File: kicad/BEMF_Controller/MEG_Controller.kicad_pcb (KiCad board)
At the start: 2 copper layers, 200 x 175 mm, 106 parts, among them J1 HEADER4VALULOK, J2 Recovery, J3 FUSE, J4 HEADER6, J5 Load, J7 Vin, Q1 C3M0280090D, Q2 C3M0280090D, Q3 C3M0280090D, Q4 C3M0280090D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

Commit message: Finished buck converter schematic
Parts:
- added C24: 100nF, Capacitor_SMD:C_0805_2012Metric, F.Cu at (381.6, 133.0)
- added C25: 6.8nF, Capacitor_SMD:C_0805_2012Metric, F.Cu at (381.6, 136.0)
- added L1: 33 uH, main:IND_BOURNS_SRN1060, F.Cu at (388.7, 113.2)
- added R1: 47k, Resistor_SMD:R_1206_3216Metric, F.Cu at (376.5, 133.1)
- added R10: 910, Resistor_SMD:R_1206_3216Metric, F.Cu at (376.5, 143.0)
- added R5: 10k, Resistor_SMD:R_1206_3216Metric, F.Cu at (376.5, 136.4)
- added R6: 20k, Resistor_SMD:R_1206_3216Metric, F.Cu at (376.5, 139.7)
- moved C69 14.1 mm to (113.8, 146.8), turned to 0 degrees
- moved C23 14.1 mm to (363.6, 90.2)
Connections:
- U1 pad 15: unconnected-(U1-PB7-Pad15) -> ConvEn
- U2 pad 3: unconnected-(U2-VC-Pad3) -> Net-(U2-VC)
- U2 pad 4: unconnected-(U2-FB-Pad4) -> /FB
- U2 pad 5: unconnected-(U2-RT-Pad5) -> Net-(U2-RT)
- U2 pad 6: unconnected-(U2-EN-Pad6) -> ConvEn
- U2 pad 7: unconnected-(U2-BST-Pad7) -> Net-(U2-BST)
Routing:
- net (no net): track 358.3 -> 22.9 mm, vias 12 -> 2
- net unconnected-(U8-OUTC-Pad13): track 191.5 -> 0.00 mm, vias 4 -> 0
- net unconnected-(U8-OUTB-Pad14): track 144.1 -> 0.40 mm, vias 4 -> 0
- net /Analog_IO/VSENSE_L_IN: track 199.7 -> 64.8 mm, vias 10 -> 6
- net /10V: track 143.4 -> 121.9 mm, vias 7 -> 5
- net GND: track 54.4 -> 44.3 mm, vias 226 -> 216
- net LOAD+: track 0.71 -> 0.00 mm

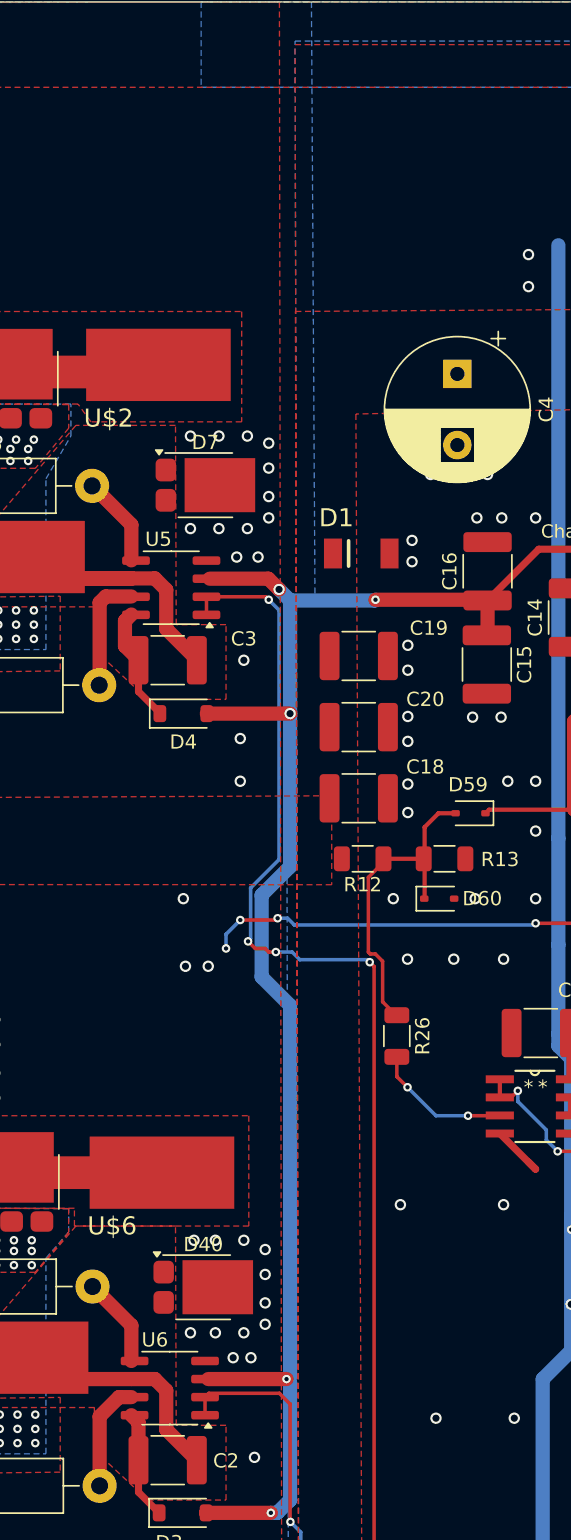
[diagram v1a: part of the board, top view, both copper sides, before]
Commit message: Updated gate drivers.
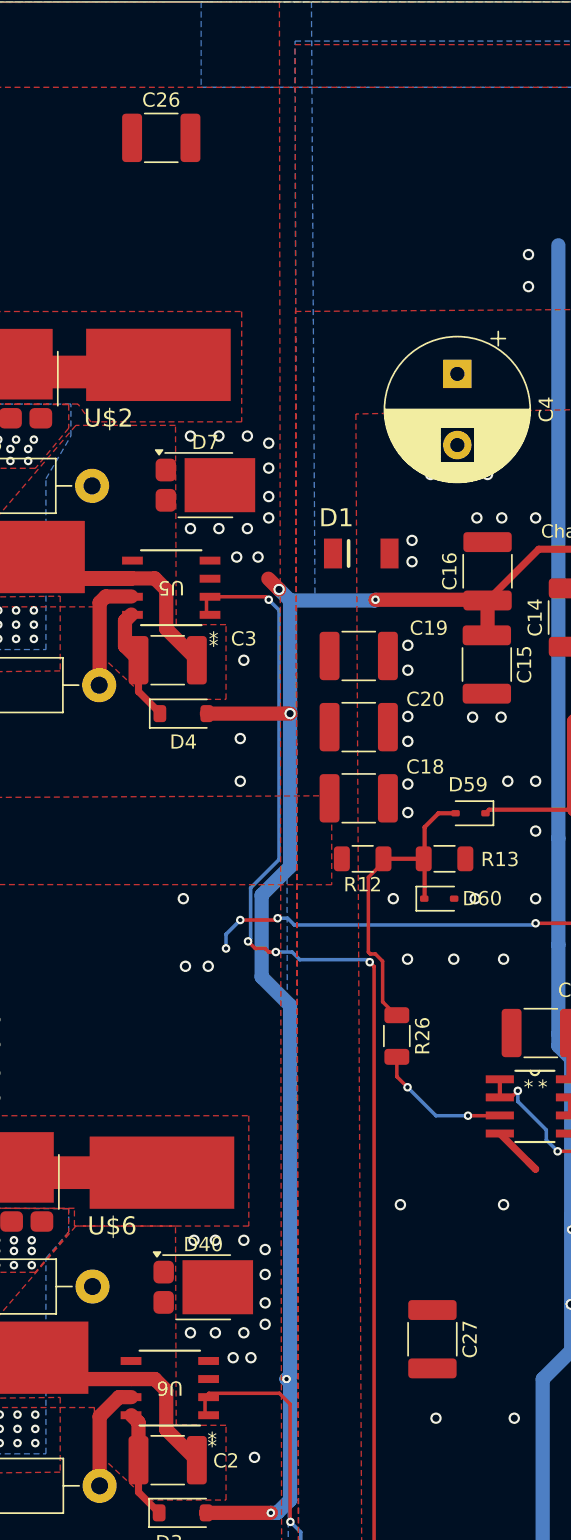
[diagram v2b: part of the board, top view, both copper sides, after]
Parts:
- added C26: 1uF, Capacitor_SMD:C_1812_4532Metric, F.Cu at (244.4, 63.3)
- added C27: 1uF, Capacitor_SMD:C_1812_4532Metric, F.Cu at (263.5, 147.7)
- U5, U6: footprint Package_SO:SOIC-8_3.9x4.9mm_P1.27mm -> main:SOICN-8_LTF
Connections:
- U5 pad 3: /10V -> GND
- U5 pad 4: GND -> /DRV_AL
- U5 pad 5: /DRV_AL -> /10V
- U6 pad 3: /10V -> GND
- U6 pad 4: GND -> /DRV_BL
- U6 pad 5: /DRV_BL -> /10V
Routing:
- net /10V: track 121.9 -> 112.3 mm
- net /DRV_AL: track 6.36 -> 0.00 mm
- net /DRV_BL: track 6.36 -> 0.00 mm

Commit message: Pretty much complete, but a few things left to do.
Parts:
- removed D54: 1N4148WS, Diode_SMD:D_SOD-323
- removed U$1: COIL_A+, main:PAD
- removed U$2, U$3, U$4, U$5, U$6: PAD, main:PAD
- added C28: 470uF, Capacitor_THT:CP_Radial_D10.0mm_P5.00mm, F.Cu at (230.5, 81.6)
- added C29: 1uF, Capacitor_SMD:C_1812_4532Metric, F.Cu at (246.3, 100.6)
- added C30: 1uF, Capacitor_SMD:C_1812_4532Metric, F.Cu at (235.2, 161.7)
- added J6: Coil_B, TerminalBlock_Phoenix:TerminalBlock_Phoenix_MKDS-1,5-2-5.08_1x02_P5.08mm_Horizontal, F.Cu at (185.6, 107.1)
- added J8: Coil_A, TerminalBlock_Phoenix:TerminalBlock_Phoenix_MKDS-1,5-2-5.08_1x02_P5.08mm_Horizontal, F.Cu at (185.5, 81.7)
- added J9: Vpower, TerminalBlock_Phoenix:TerminalBlock_Phoenix_MKDS-1,5-2-5.08_1x02_P5.08mm_Horizontal, F.Cu at (281.3, 55.5)
- C14: value 1uF -> 470uF; footprint Capacitor_SMD:C_1812_4532Metric -> Capacitor_THT:CP_Radial_D10.0mm_P5.00mm
- J1: footprint main:4PINVALULOK -> TerminalBlock_Phoenix:TerminalBlock_Phoenix_MKDS-1,5-4-5.08_1x04_P5.08mm_Horizontal
- J4: footprint main:6PINVALULOK -> TerminalBlock_Phoenix:TerminalBlock_Phoenix_MKDS-1,5-6_1x06_P5.00mm_Horizontal
- Q1, Q2, Q3, Q4: footprint Package_TO_SOT_THT:TO-247-3_Horizontal_TabDown -> Package_TO_SOT_THT:TO-247-3_Vertical
- R14, R15, R16, R17: value 10 -> 2R2; footprint Resistor_THT:R_Axial_DIN0411_L9.9mm_D3.6mm_P15.24mm_Horizontal -> Resistor_SMD:R_1206_3216Metric
- U3: value V_REG_78XX -> V_REG_7805
- U4: value TC1240A -> V_REG_7810; footprint main:SOT23-6 -> main:V78W_BACKWARDS
- moved R1 202.7 mm to (190.1, 53.6), turned to 90 degrees
- moved C24 200.4 mm to (193.3, 64.3)
- moved C25 198.9 mm to (198.6, 58.0), turned to 90 degrees
- moved D13 197.6 mm to (183.4, 141.1), turned to 90 degrees
- moved R5 196.3 mm to (198.6, 53.5), turned to 90 degrees
- moved R10 191.7 mm to (207.7, 52.1)
- moved D12 188.1 mm to (190.7, 142.2), turned to 180 degrees
- moved D10 187.7 mm to (183.2, 161.0), turned to -90 degrees
- moved R6 185.2 mm to (213.4, 52.0), turned to 180 degrees
- moved L1 180.2 mm to (216.5, 60.0)
- moved D8 179.0 mm to (190.8, 160.5), turned to 180 degrees
- moved C8 173.1 mm to (183.8, 53.9), turned to 180 degrees
- moved J2 172.1 mm to (185.8, 148.8), turned to -90 degrees
- moved U2 171.9 mm to (193.2, 59.9), turned to 180 degrees
- moved C7 168.9 mm to (183.8, 58.8), turned to 180 degrees
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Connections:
- net Net-(D12-K) renamed /REC_B
- net Net-(D8-K) renamed /REC_A
- C14 pad 1: Net-(U4-C-) -> 5V
- C14 pad 2: Net-(U4-C+) -> GND
- C15 pad 1: /10V -> +10V
- C16 pad 1: /10V -> 5V
- C26 pad 2: /10V -> +10V
- C27 pad 2: /10V -> +10V
- D3 pad 2: /10V -> +10V
- D4 pad 2: /10V -> +10V
- R41 pad 1: Net-(D54-A) -> /Analog_IO/VSENSE_L_IN
- U1 pad 13: /B_O -> unconnected-(U1-PB5-Pad13)
- U1 pad 14: /A_O -> unconnected-(U1-PB6-Pad14)
- U1 pad 15: ConvEn -> unconnected-(U1-PB7-Pad15)
- U1 pad 16: unconnected-(U1-PB8-Pad16) -> /B_O
- U1 pad 17: unconnected-(U1-PB9-Pad17) -> /A_O
- U1 pad 24: unconnected-(U1-PC15-Pad24) -> ConvEn
- U1 pad 28: DUTY -> HALL_1_IN
- U1 pad 29: THROTTLE -> HALL_2_IN
- U1 pad 30: unconnected-(U1-PA4-Pad30) -> HALL_3_IN
- U1 pad 31: unconnected-(U1-PA5-Pad31) -> HALL_4_IN
- U1 pad 32: HALL_1_IN -> THROTTLE
- U1 pad 33: HALL_2_IN -> DUTY
- U1 pad 34: HALL_3_IN -> unconnected-(U1-PB0-Pad34)
- U1 pad 35: HALL_4_IN -> unconnected-(U1-PB1-Pad35)
- U2 pad 6: ConvEn -> ConvEnIso
- U5 pad 5: /10V -> +10V
- U6 pad 5: /10V -> +10V
- U8 pad 12: unconnected-(U8-OUTD-Pad12) -> ConvEnIso
- U8 pad 5: unconnected-(U8-IND-Pad5) -> ConvEn
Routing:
- net LOAD+: track 0.00 -> 180.2 mm, vias 0 -> 4
- net V_RAW: track 29.0 -> 196.3 mm, vias 37 -> 0
- net 5V: track 223.6 -> 346.3 mm, vias 5 -> 3
- net /10V: track 112.3 -> 0.00 mm, vias 5 -> 0
- net ConvEnIso: track 0.00 -> 91.5 mm, vias 0 -> 4
- net +10V: track 0.00 -> 85.3 mm, vias 0 -> 3
- net 3.3V: track 224.7 -> 147.3 mm, vias 6 -> 4
- net GND: track 44.3 -> 119.5 mm, vias 216 -> 263
- net /CTRL_A: track 99.6 -> 30.3 mm, vias 4 -> 0
- net HALL_1_IN: track 0.00 -> 61.2 mm
- net Net-(J7-Pin_1): track 24.9 -> 82.7 mm
- net HALL_2_IN: track 0.00 -> 54.9 mm
- net HALL_3_IN: track 0.00 -> 49.1 mm
- net HALL_4_IN: track 0.00 -> 43.2 mm
- net Net-(D2-K): track 0.00 -> 40.4 mm
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- added copper zone on F.Cu, net LOAD+
- removed copper zone on F.Cu, net COIL_A_+
- removed copper zone on F.Cu, net COIL_A_-
- removed copper zone on F.Cu, net COIL_B_+
- removed copper zone on F.Cu, net COIL_B_-
- removed copper zone on F.Cu, net Net-(J9-Pin_1)
- removed copper zone on B.Cu, net V_RAW
- removed copper zone on F.Cu, net V_RAW
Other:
- board size 200 x 175 mm -> 110 x 120 mm
- board text added: "Analog inputs"
- board text added: "MEG Controller1.0 Designed by Lamare, Okt 2024"
- board text added: "Pot"
- board text added: "Pot inputs"
- board text removed: "A Halls"
- board text removed: "BEMF Controller1.0 Designed by Lamare, Jul 2024"
- board text removed: "Charge Pump"
- board text removed: "DUTY"
- board text removed: "Throttle"
- board text removed: "VIN"
